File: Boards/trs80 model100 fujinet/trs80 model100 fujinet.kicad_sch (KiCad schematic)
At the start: 17 parts

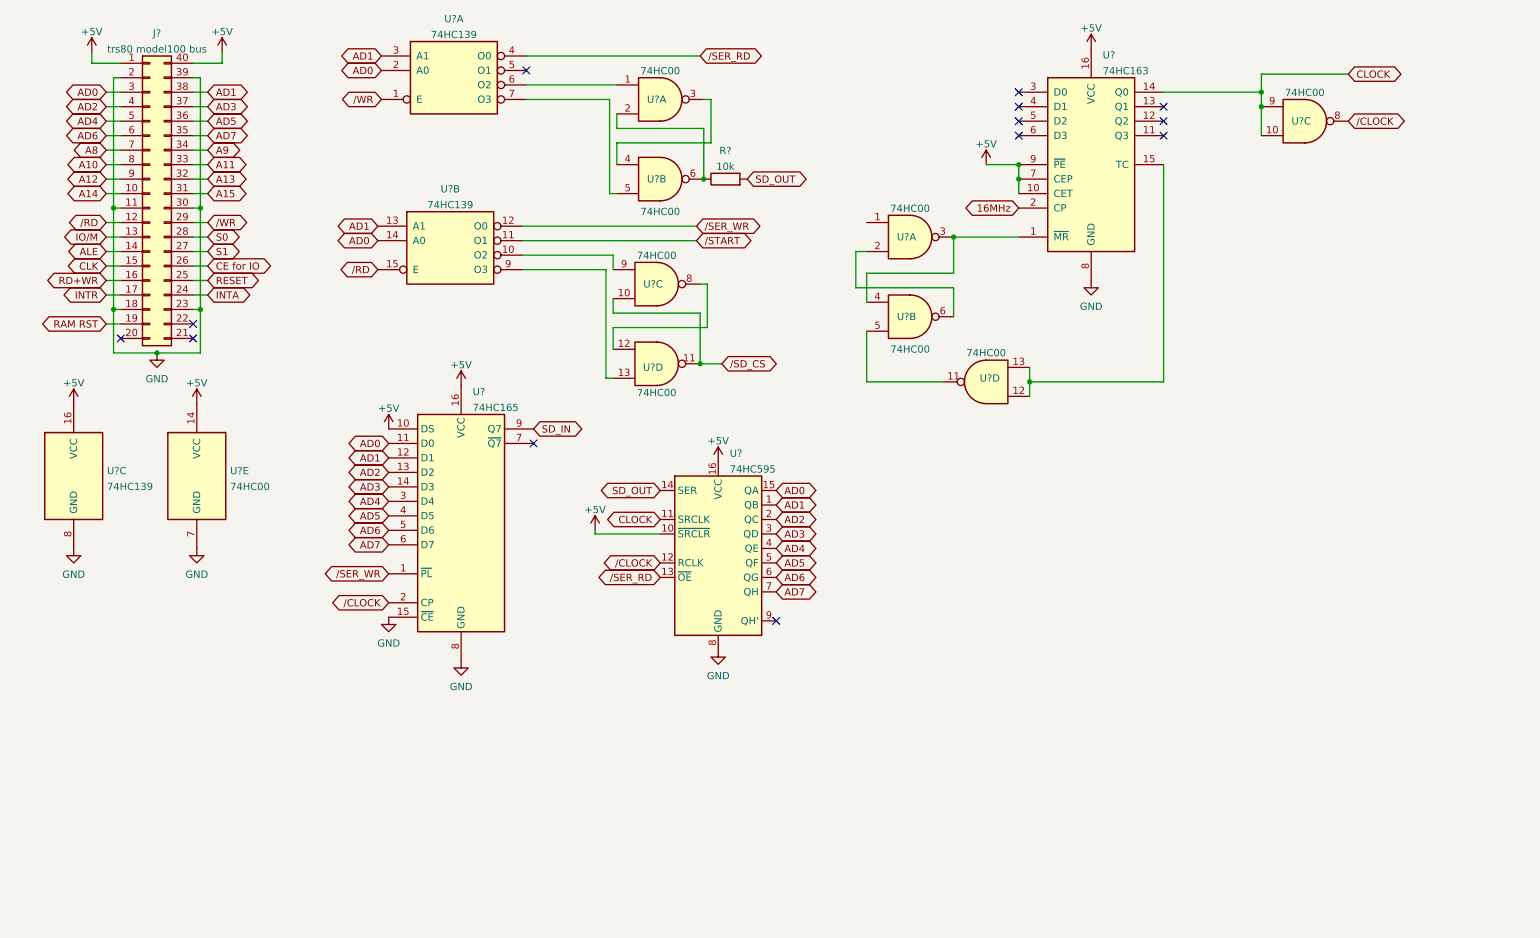
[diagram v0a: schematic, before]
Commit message: tweaked bus interface for 8085
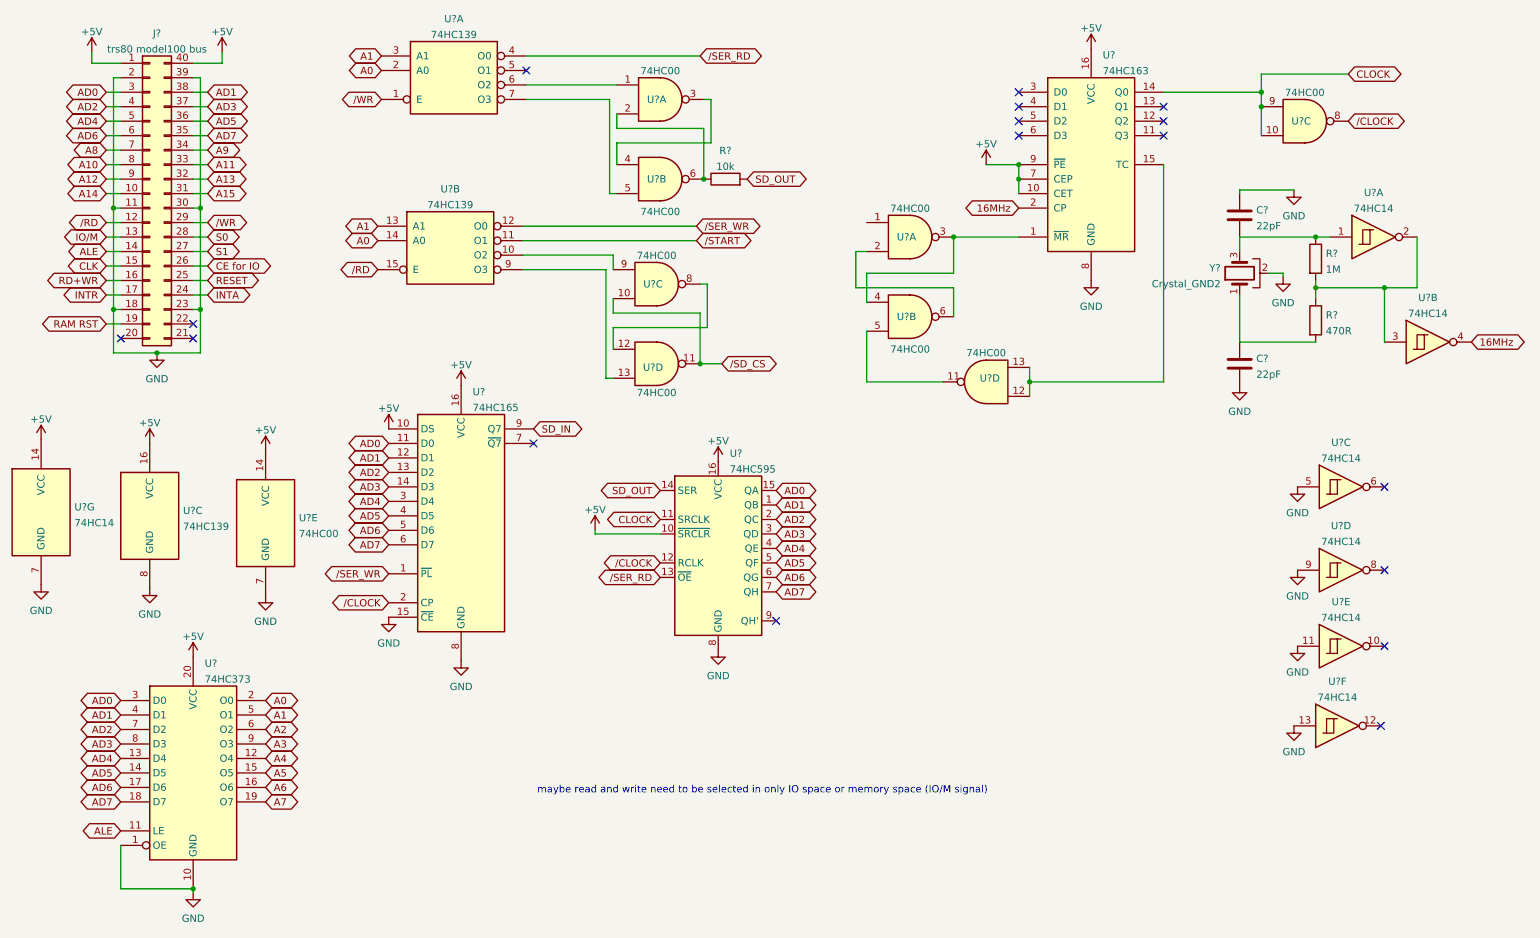
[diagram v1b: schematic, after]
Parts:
- added C? (x2): 22pF, symbol Device:C
- added R?: 470R, symbol Device:R
- added R?: 1M, symbol Device:R
- added U? (x7): 74HC14, symbol 74xx:74HC14
- added U?: 74HC373, symbol 74xx:74HC373
- added Y?: Crystal_GND2, symbol Device:Crystal_GND2
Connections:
- net +5V: now also U?.14 (VCC), U?.20 (VCC)
- net 16MHz: now also U?.4
- net AD0: now also U?.3 (D0); no longer U?.14 (A0), U?.2 (A0)
- net AD1: now also U?.4 (D1); no longer U?.13 (A1), U?.3 (A1)
- net AD2: now also U?.7 (D2)
- net AD3: now also U?.8 (D3)
- net AD4: now also U?.13 (D4)
- net AD5: now also U?.14 (D5)
- net AD6: now also U?.17 (D6)
- net AD7: now also U?.18 (D7)
- net ALE: now also U?.11 (LE)
- net GND: now also C?.1, C?.2, U?.1 (OE), U?.10 (GND), U?.11, U?.13, U?.5, U?.7 (GND), U?.9, Y?.2
- new net: C?.1, R?.2, Y?.1
- new net: R?.1, R?.2, U?.2, U?.3
- new net: C?.2, R?.1, U?.1, Y?.3
- new net A0: U?.14 (A0), U?.2 (A0), U?.2 (O0)
- new net A1: U?.13 (A1), U?.3 (A1), U?.5 (O1)
- new net A2: U?.6 (O2)
- new net A3: U?.9 (O3)
- new net A4: U?.12 (O4)
- new net A5: U?.15 (O5)
- new net A6: U?.16 (O6)
- new net A7: U?.19 (O7)
- no-connect marks 13 -> 17
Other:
- note added: "maybe read and write need to be selected in only IO space or memory space (IO/M signal)"
- moved on the sheet: U?C, U?E
